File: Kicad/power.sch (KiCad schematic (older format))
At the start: 13 parts, among them J401 USB_B, SW401 SW_Push_DPDT_ON_OFF, SW402 SW_Push_DPDT_ON_MO, U401 TC1262-33

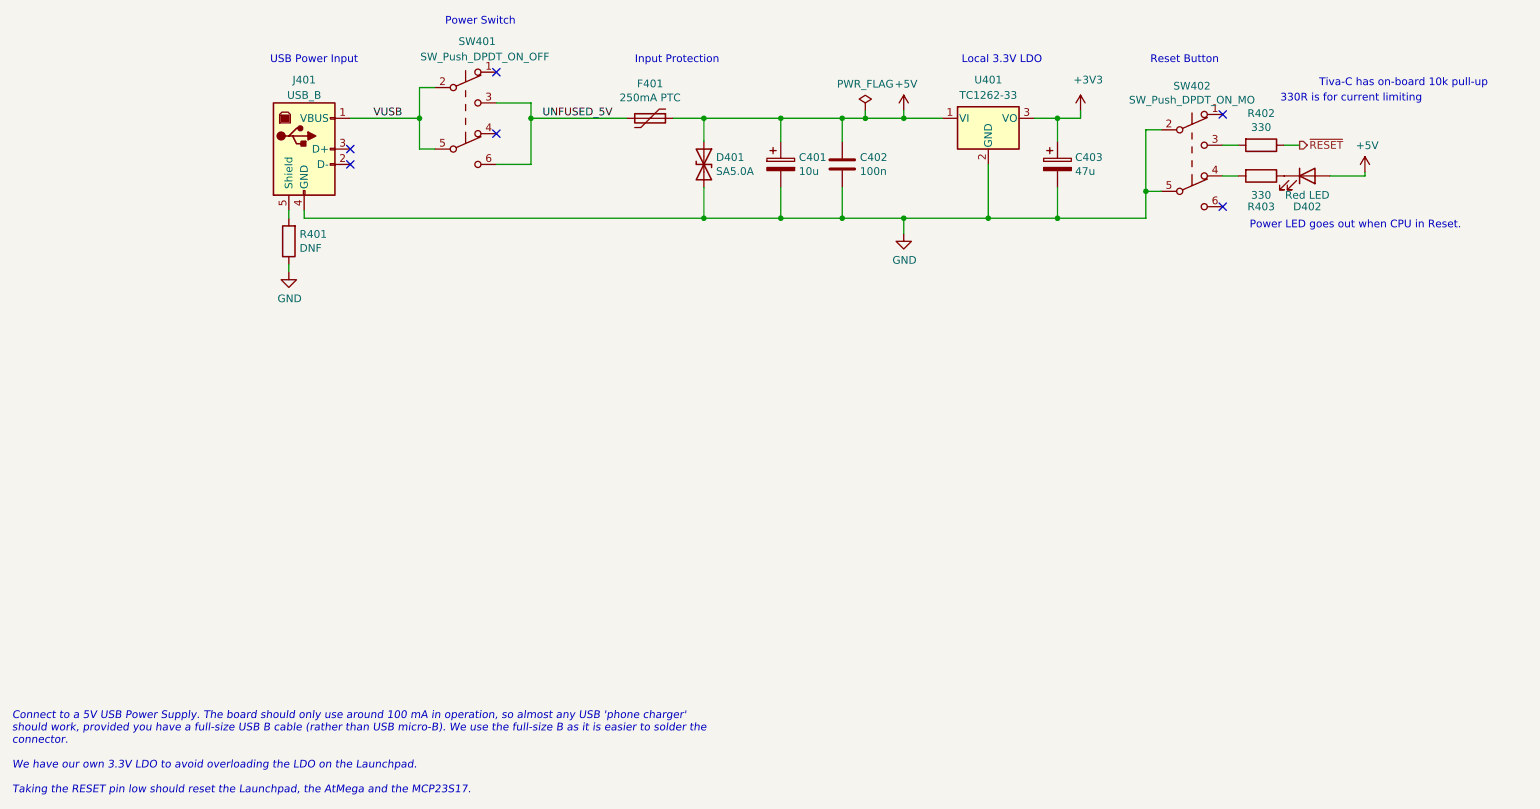
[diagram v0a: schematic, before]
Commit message: Switch to 1598D enclosure.
Use MIC2005A current limiter on input.
Use soft on/off switch from Atmega.
Atmega connects to Tiva over I2C.
Use full-size SD card.
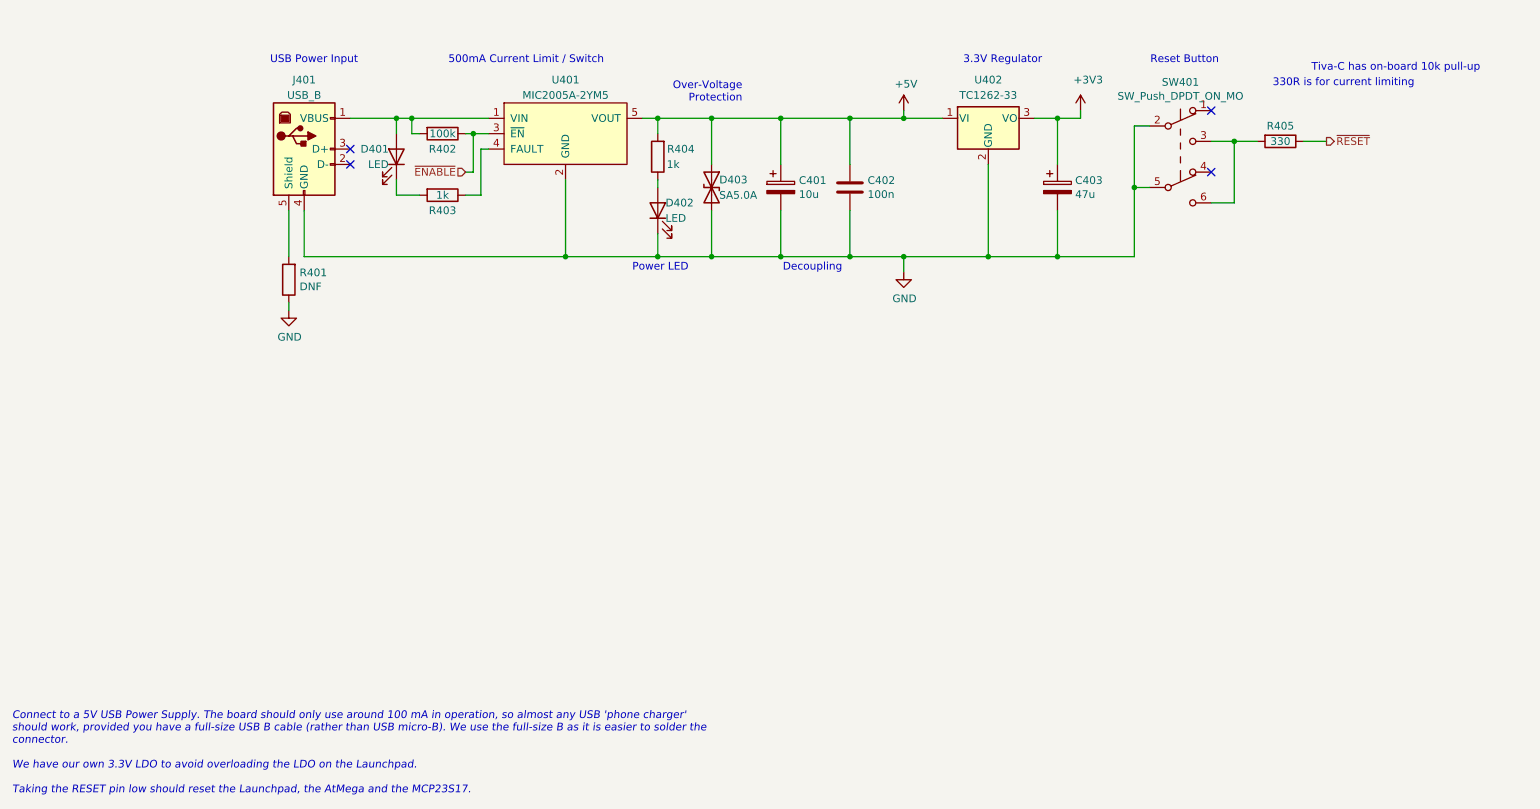
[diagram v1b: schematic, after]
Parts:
- removed F401: 250mA PTC, Fuse:Fuse_Littelfuse_395Series, symbol Device:Polyfuse
- removed SW401: SW_Push_DPDT_ON_OFF, Neotron 32:PHB2UEETS1A, symbol Switch:SW_Push_DPDT
- added D401: LED, LED_THT:LED_D3.0mm, symbol Device:LED
- added R402: 100k, Resistor_THT:R_Axial_DIN0207_L6.3mm_D2.5mm_P10.16mm_Horizontal, symbol Device:R
- added R404: 1k, Resistor_THT:R_Axial_DIN0207_L6.3mm_D2.5mm_P10.16mm_Horizontal, symbol Device:R
- added U401: MIC2005A-2YM5, Package_TO_SOT_SMD:SOT-23-5_HandSoldering, symbol neotron-32:MIC2005A-2YM5
- D402: value Red LED -> LED; DNP 0 -> (none); Manufacturer Würth Elektronik -> (none); mpn 151031SS04000 -> (none)
- R403: value 330 -> 1k; DNP 0 -> (none); Manufacturer Stackpole Electronics Inc -> (none); digikey# CF14JT330RCT-ND -> (none); mpn CF14JT330R -> (none)
- renumbered D401 to D403, R402 to R405, SW402 to SW401, U401 to U402
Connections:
- net +5V: now also R404.2, U401.5 (VOUT); no longer D402.2 (A)
- net GND: now also D402.1 (K), U401.2 (GND)
- net at R405.2, SW401.3 (C): now also SW401.6 (C)
- net at SW401.4 (A): no longer R403.2
- net at R403.1: now also U401.4 (FAULT); no longer D402.1 (K)
- net VUSB: no longer names the net of J401.1 (VBUS)
- net VUSB: now also D401.2 (A), R402.2, U401.1 (VIN)
- new net: D401.1 (K), R403.2
- new net: D402.2 (A), R404.1
- new net ~ENABLE: R402.1, U401.3 (~EN)
- no-connect marks 6 -> 4
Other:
- note added: "3.3V Regulator"
- note added: "500mA Current Limit / Switch"
- note added: "Decoupling"
- note added: "Over-Voltage\nProtection"
- note added: "Power LED"
- note removed: "Input Protection"
- note removed: "Local 3.3V LDO"
- note removed: "Power LED goes out when CPU in Reset."
- note removed: "Power Switch"
- moved on the sheet: C401, C402, C403, D403, R401, R405, SW401
